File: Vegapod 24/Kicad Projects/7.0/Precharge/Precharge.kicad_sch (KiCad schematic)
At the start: 53 parts, among them J1 VCU, J2 E-Stop, J3 LV Supply, J4 Intertial Switch, J5 Contactor1, J6 DCV, J7 Contactor2, J8 24V IN, K1 Relay_SPDT, K2 Relay_SPDT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

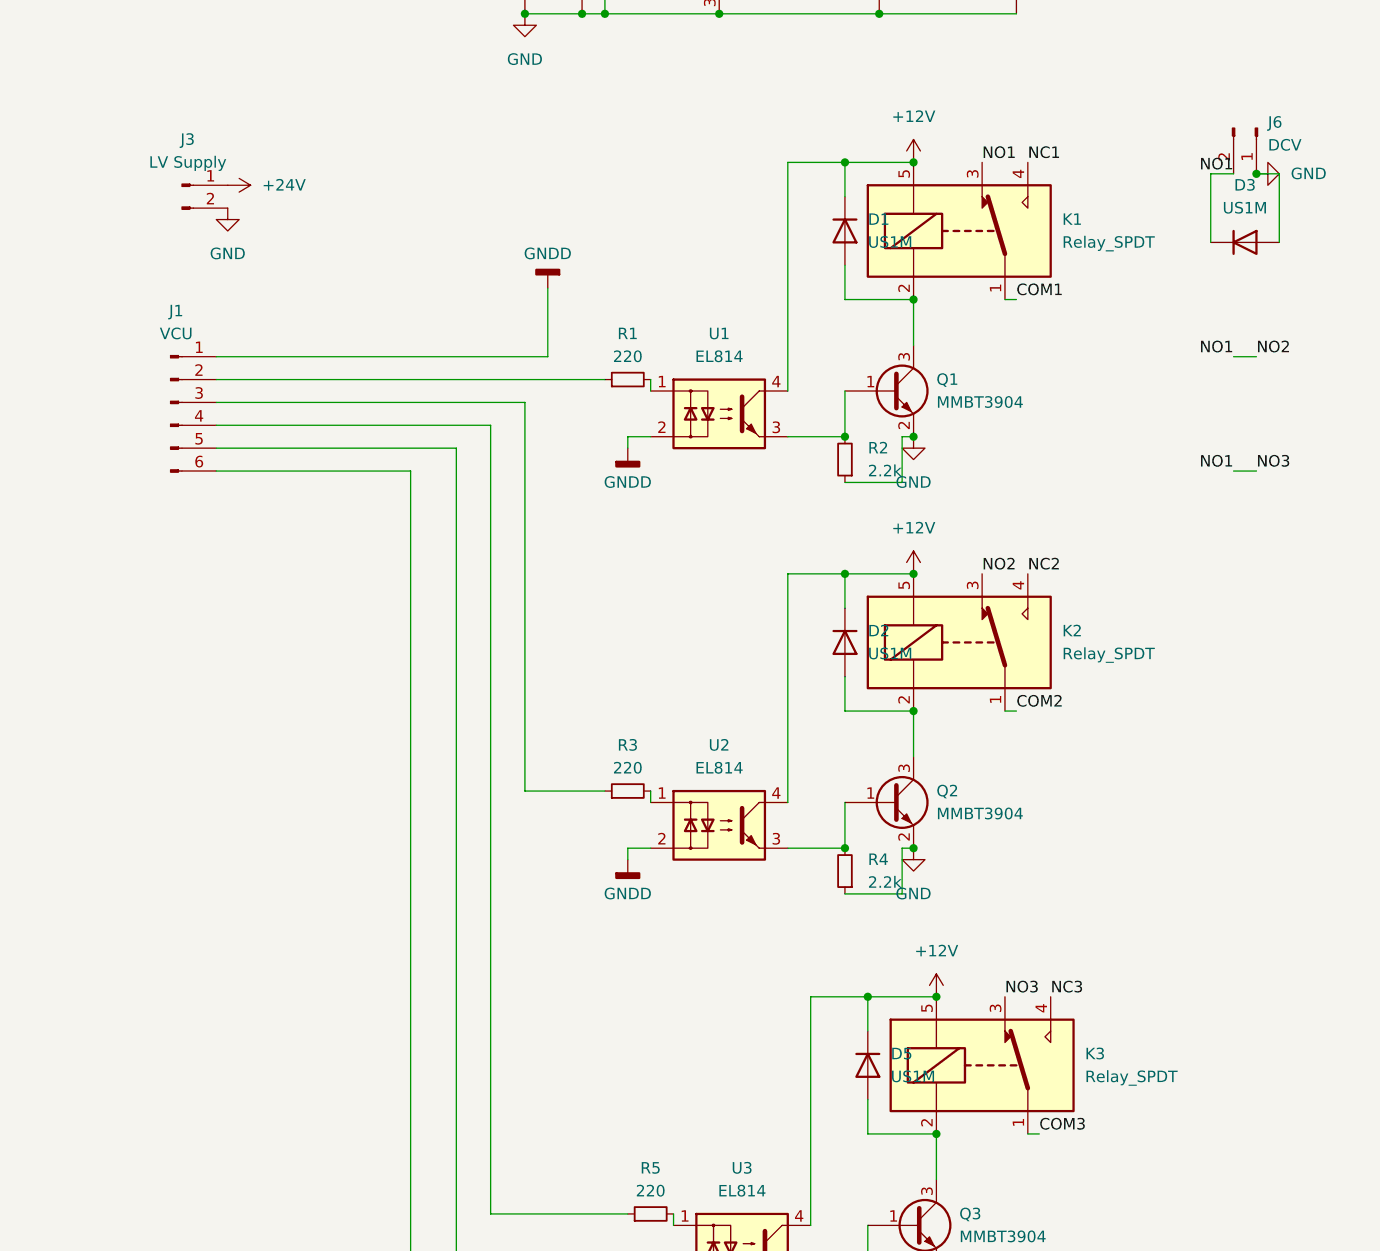
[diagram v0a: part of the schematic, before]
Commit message: Added IMD Support to interlock
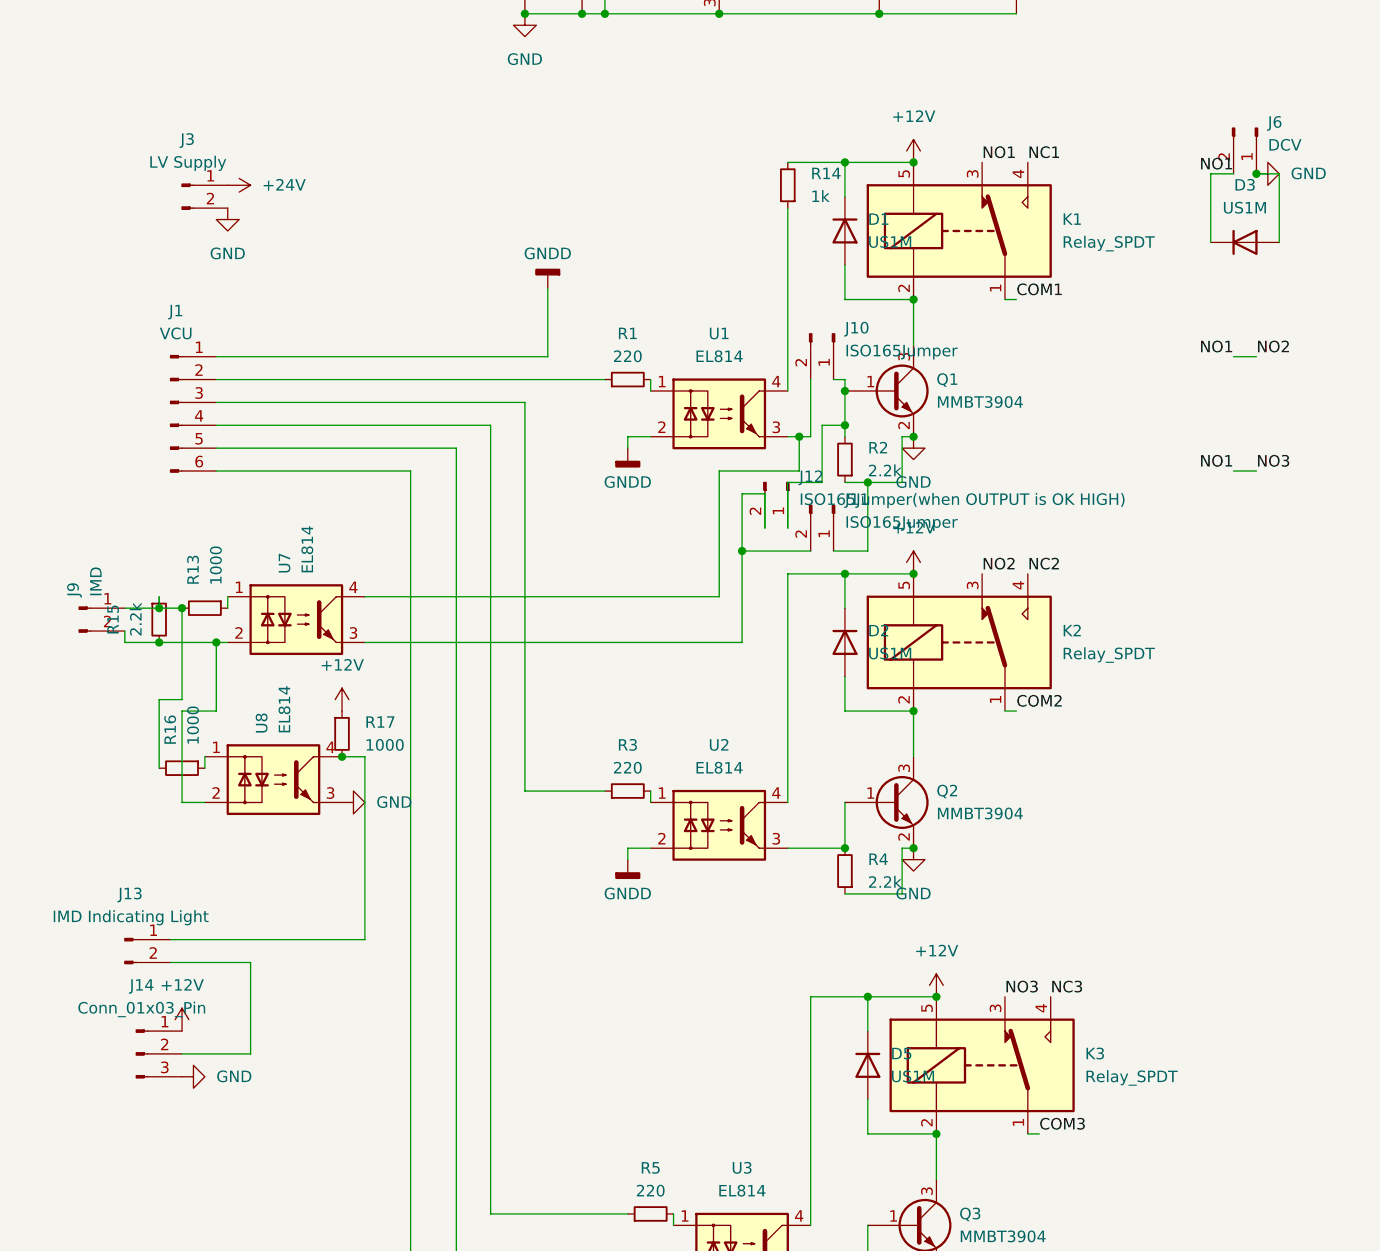
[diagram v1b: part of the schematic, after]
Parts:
- added J10, J11: ISO165Jumper, Connector_PinHeader_1.27mm:PinHeader_1x02_P1.27mm_Vertical, symbol Connector:Conn_01x02_Pin
- added J12: ISO165Jumper(when OUTPUT is OK HIGH), Connector_PinHeader_1.27mm:PinHeader_1x02_P1.27mm_Vertical, symbol Connector:Conn_01x02_Pin
- added J13: IMD Indicating Light, Connector_Phoenix_MC_HighVoltage:PhoenixContact_MCV_1,5_2-G-5.08_1x02_P5.08mm_Vertical, symbol Connector:Conn_01x02_Pin
- added J14: Conn_01x03_Pin, Connector_PinHeader_1.27mm:PinHeader_1x03_P1.27mm_Vertical, symbol Connector:Conn_01x03_Pin
- added J9: IMD, Connector_PinHeader_2.54mm:PinHeader_1x02_P2.54mm_Vertical, symbol Connector:Conn_01x02_Pin
- added R13, R16, R17: 1000, Resistor_SMD:R_0805_2012Metric_Pad1.20x1.40mm_HandSolder, symbol Device:R_Small
- added R14: 1k, Resistor_SMD:R_0805_2012Metric_Pad1.20x1.40mm_HandSolder, symbol Device:R_Small
- added R15: 2.2k, Resistor_SMD:R_0805_2012Metric_Pad1.20x1.40mm_HandSolder, symbol Device:R_Small
- added U7, U8: EL814, Package_DIP:SMDIP-4_W9.53mm, symbol Isolator:EL814
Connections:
- net +12V: now also J14.1 (Pin_1), R14.2, R17.1; no longer U1.4
- net GND: now also J11.1 (Pin_1), J14.3 (Pin_3), U8.3
- net at Q1.1 (B), R2.2: now also J10.1 (Pin_1), J12.1 (Pin_1); no longer U1.3
- new net: R16.1, U8.1
- new net: J9.2 (Pin_2), R15.2, U7.2, U8.2
- new net: J13.1 (Pin_1), R17.2, U8.4
- new net: R14.1, U1.4
- new net: J11.2 (Pin_2), J12.2 (Pin_2), U7.3
- new net: J9.1 (Pin_1), R13.2, R15.1, R16.2
- new net: R13.1, U7.1
- new net: J10.2 (Pin_2), U1.3, U7.4
- new net: J13.2 (Pin_2), J14.2 (Pin_2)
